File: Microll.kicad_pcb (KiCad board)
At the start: 2 copper layers, 41.1 x 57.9 mm, 35 parts, among them J1 Conn_02x08_Top_Bottom, J3 Conn_01x08, J4 USB_C_Receptacle, J5 Conn_01x08, SW1 SW_Push, SW2 SW_Push, SW3 SW_Push, U1 ESP32-C3-WROOM-02-N4, U2 TLV76733DRVx, U3 STM32G0B1CBU6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

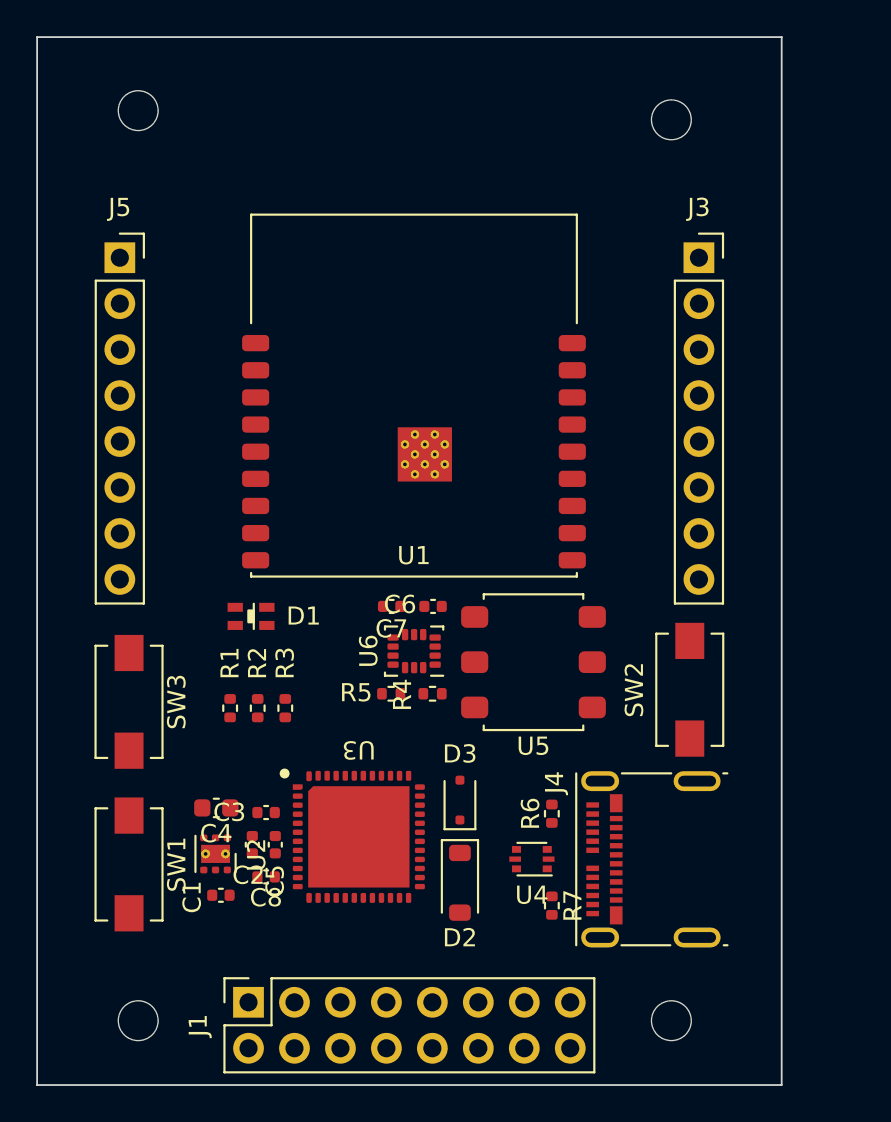
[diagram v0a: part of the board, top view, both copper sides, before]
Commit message: Changed the programming switches to a more compact dip format to save board space
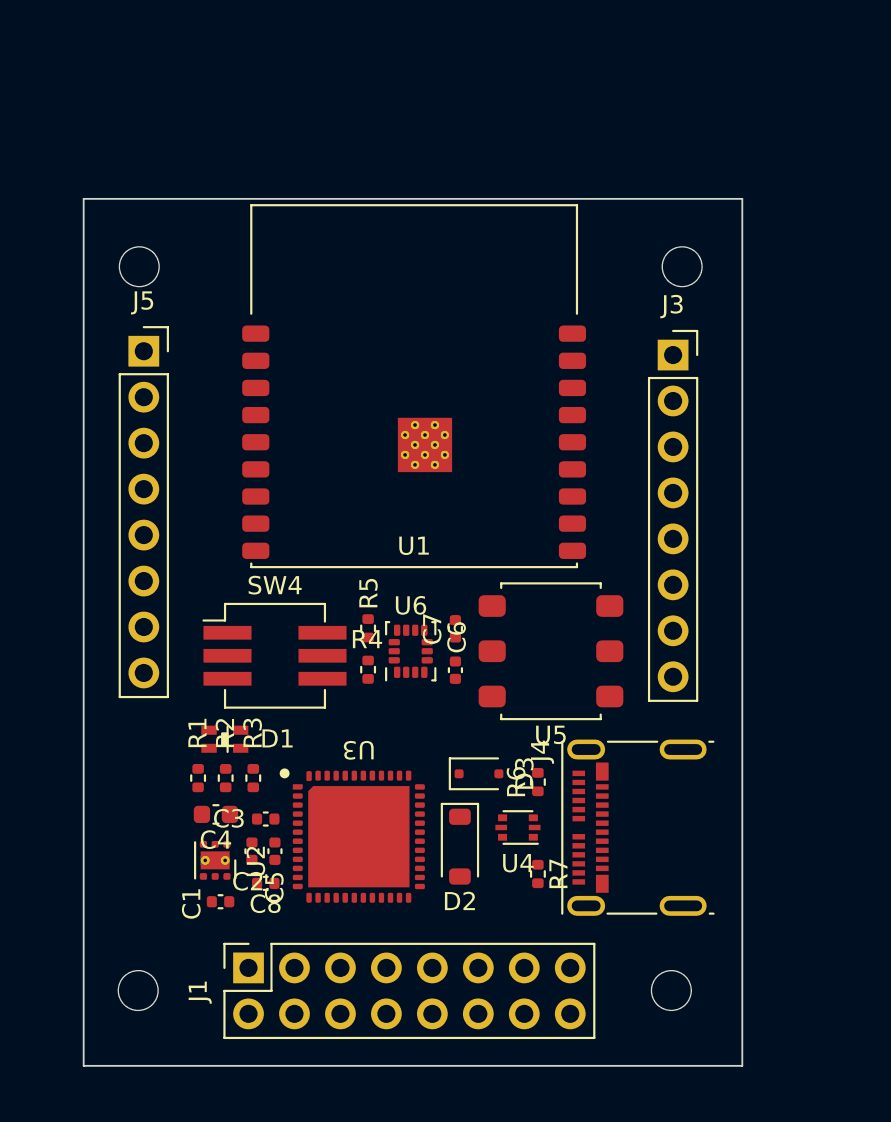
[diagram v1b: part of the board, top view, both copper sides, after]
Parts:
- removed SW1, SW2, SW3: SW_Push, Button_Switch_SMD:SW_SPST_EVQPE1
- added SW4: SW_DIP_x03, Button_Switch_SMD:SW_DIP_SPSTx03_Slide_KingTek_DSHP03TJ_W5.25mm_P1.27mm_JPin, F.Cu at (99.0, 69.8)
- moved H1 8.63 mm to (91.5, 48.2)
- moved H3 8.14 mm to (121.5, 48.2)
- moved D1 6.94 mm to (96.2, 74.4)
- moved J3 5.56 mm to (121.0, 53.1)
- moved J5 5.34 mm to (91.8, 52.9)
- moved R1 4.25 mm to (94.8, 76.5)
- moved R2 4.25 mm to (96.3, 76.5)
- moved R3 4.25 mm to (97.8, 76.5)
- moved R5 3.84 mm to (104.1, 68.2), turned to -90 degrees
- moved R4 3.80 mm to (104.1, 70.5), turned to 90 degrees
- moved C6 3.73 mm to (109.0, 70.5), turned to 90 degrees
- moved C7 3.73 mm to (109.0, 68.3), turned to -90 degrees
- moved D2 2.00 mm to (109.2, 80.3)
- moved J4 1.91 mm to (119.0, 79.2)
- moved R7 1.91 mm to (113.5, 81.8)
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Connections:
- U1 pad 2: +3.3V -> /EN
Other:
- board size 41.1 x 57.9 mm -> 36.4 x 47.9 mm

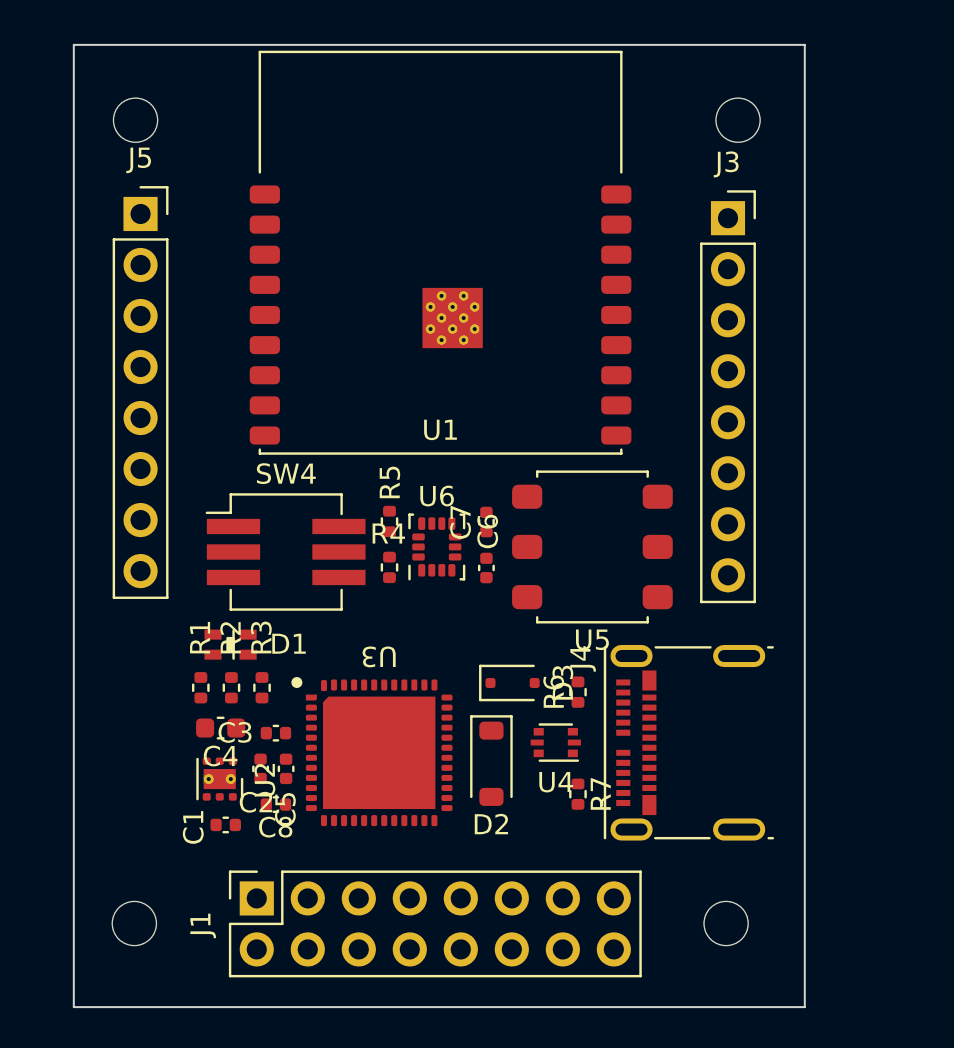
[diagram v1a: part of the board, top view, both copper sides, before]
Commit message: Board outline defined. Initial routing comenced
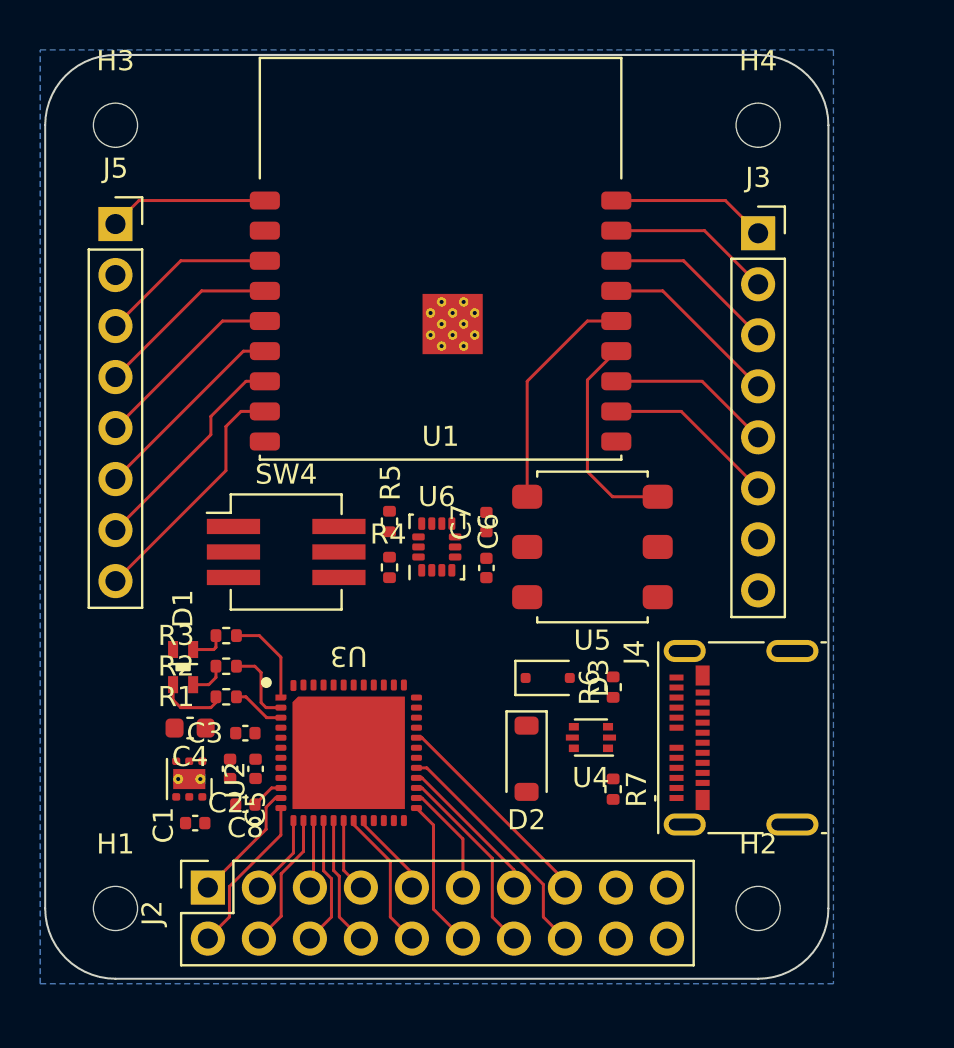
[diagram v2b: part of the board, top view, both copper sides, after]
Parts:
- removed J1: Conn_02x08_Top_Bottom, Connector_PinSocket_2.54mm:PinSocket_2x08_P2.54mm_Vertical
- added J2: Conn_02x10_Top_Bottom, Connector_PinSocket_2.54mm:PinSocket_2x10_P2.54mm_Vertical, F.Cu at (95.1, 86.5)
- moved H4 50.4 mm to (122.5, 48.5)
- moved H1 39.3 mm to (90.5, 87.5)
- moved H3 31.0 mm to (90.5, 48.5)
- moved R3 3.15 mm to (96.0, 73.9), turned to 0 degrees
- moved J4 2.66 mm to (121.7, 79.0)
- moved D1 2.61 mm to (93.9, 75.5), turned to 90 degrees
- moved D2 1.77 mm to (111.0, 80.0)
- moved D3 1.77 mm to (112.0, 76.0)
- moved R6 1.77 mm to (115.3, 76.5)
- moved R7 1.77 mm to (115.3, 81.6)
- moved U4 1.77 mm to (114.2, 79.0)
- moved H2 1.76 mm to (122.5, 87.5)
- moved J3 1.68 mm to (122.5, 53.9)
- moved C1 1.52 mm to (94.5, 83.2)
- moved C2 1.52 mm to (96.2, 80.5)
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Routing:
- net /GPIO9: track 0.00 -> 12.2 mm
- net USART_TX: track 0.00 -> 11.9 mm
- net ESP32_USB+: track 0.00 -> 11.4 mm
- net /GPIO8: track 0.00 -> 11.0 mm
- net USART_RX: track 0.00 -> 10.7 mm
- net ESP32_USB-: track 0.00 -> 10.6 mm
- net /GPIO7: track 0.00 -> 10.1 mm
- net /PB15: track 0.00 -> 9.67 mm
- net /GPIO6: track 0.00 -> 9.65 mm
- net SCL: track 0.00 -> 9.21 mm
- net /GPIO3: track 0.00 -> 9.03 mm
- net SDA: track 0.00 -> 8.78 mm
- net /Rx: track 0.00 -> 8.65 mm
- net /GPIO2: track 0.00 -> 8.60 mm
- net /Tx: track 0.00 -> 8.22 mm
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- added copper zone on B.Cu, net GND
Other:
- board size 36.4 x 47.9 mm -> 39 x 46 mm

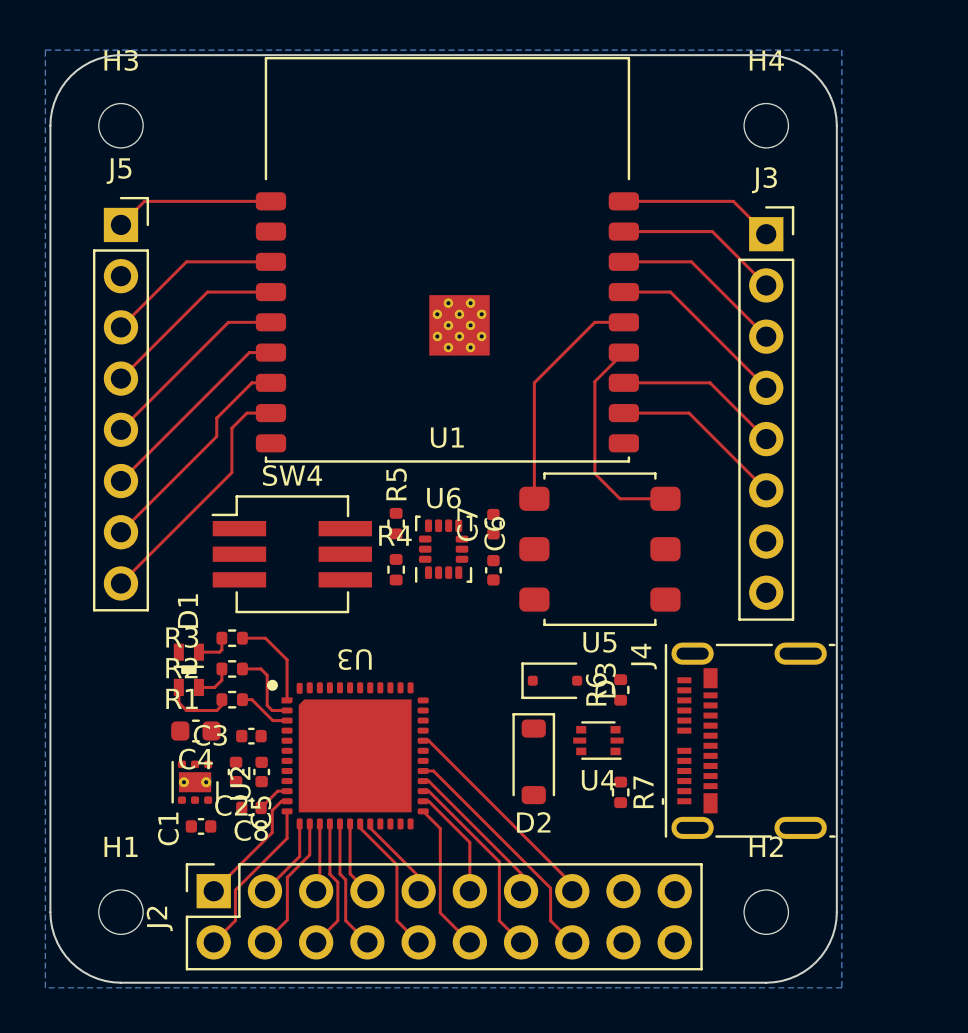
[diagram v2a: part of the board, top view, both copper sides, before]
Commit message: Additional routing. Need to update power symbols due tto kicad 8. Need to add 4 pins from STM32
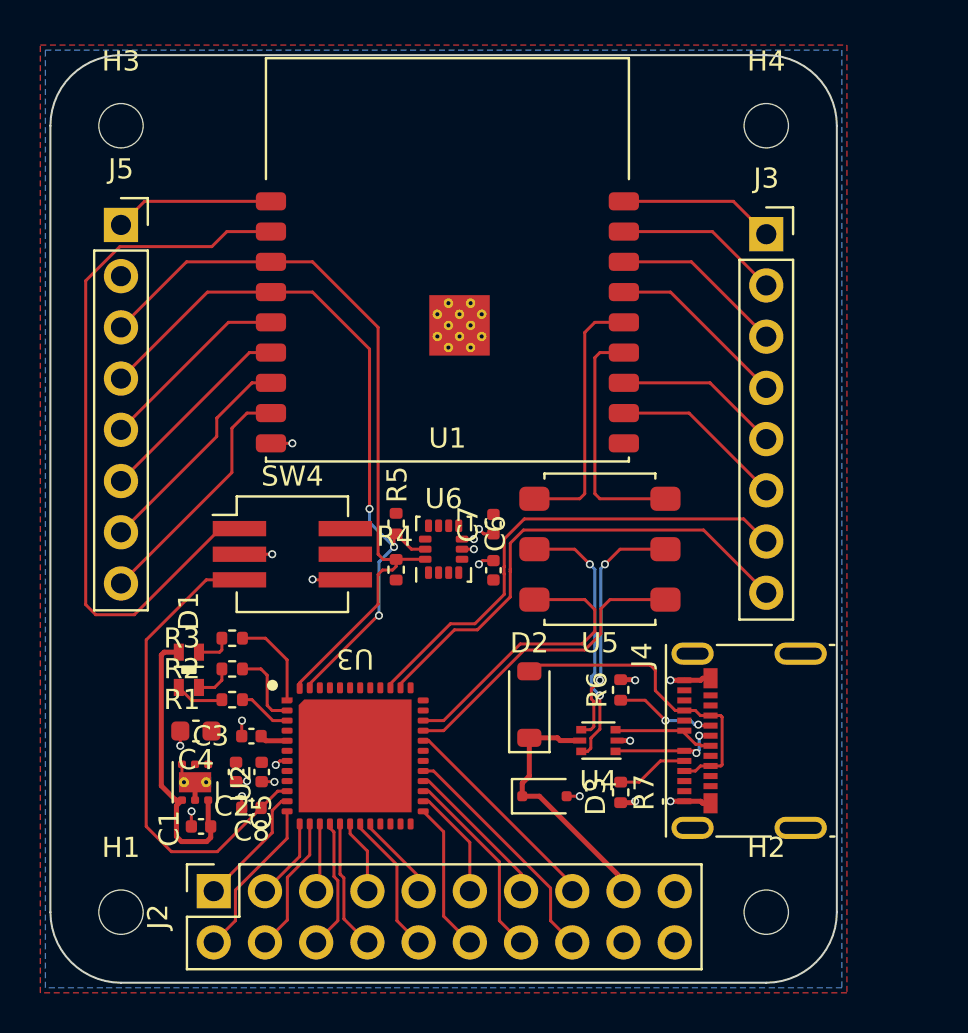
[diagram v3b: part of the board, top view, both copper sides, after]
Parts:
- moved D3 5.75 mm to (111.5, 81.8)
- moved D2 2.85 mm to (110.8, 77.2), turned to 90 degrees
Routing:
- net /EN: track 0.00 -> 35.9 mm
- net SDA: track 8.78 -> 37.8 mm
- net SCL: track 9.21 -> 36.8 mm, vias 0 -> 3
- net +5V: track 0.00 -> 27.3 mm
- net CAN_RX: track 0.00 -> 24.4 mm
- net CAN_TX: track 0.00 -> 24.3 mm
- net /RESET: track 1.63 -> 23.9 mm
- net GND: track 0.00 -> 20.5 mm, vias 0 -> 20
- net /5V_bus: track 0.00 -> 15.7 mm
- net STM32_USB-: track 0.00 -> 15.4 mm
- net STM32_USB+: track 0.00 -> 14.6 mm
- net /USB+: track 0.00 -> 13.3 mm, vias 0 -> 2
- net /USB-: track 0.00 -> 12.4 mm, vias 0 -> 2
- net /D+: track 0.00 -> 5.55 mm, vias 0 -> 2
- net /D-: track 0.00 -> 5.11 mm
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- added copper zone on F.Cu, net +3.3V
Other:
- board text added: "Remember to break out these 4 pins"

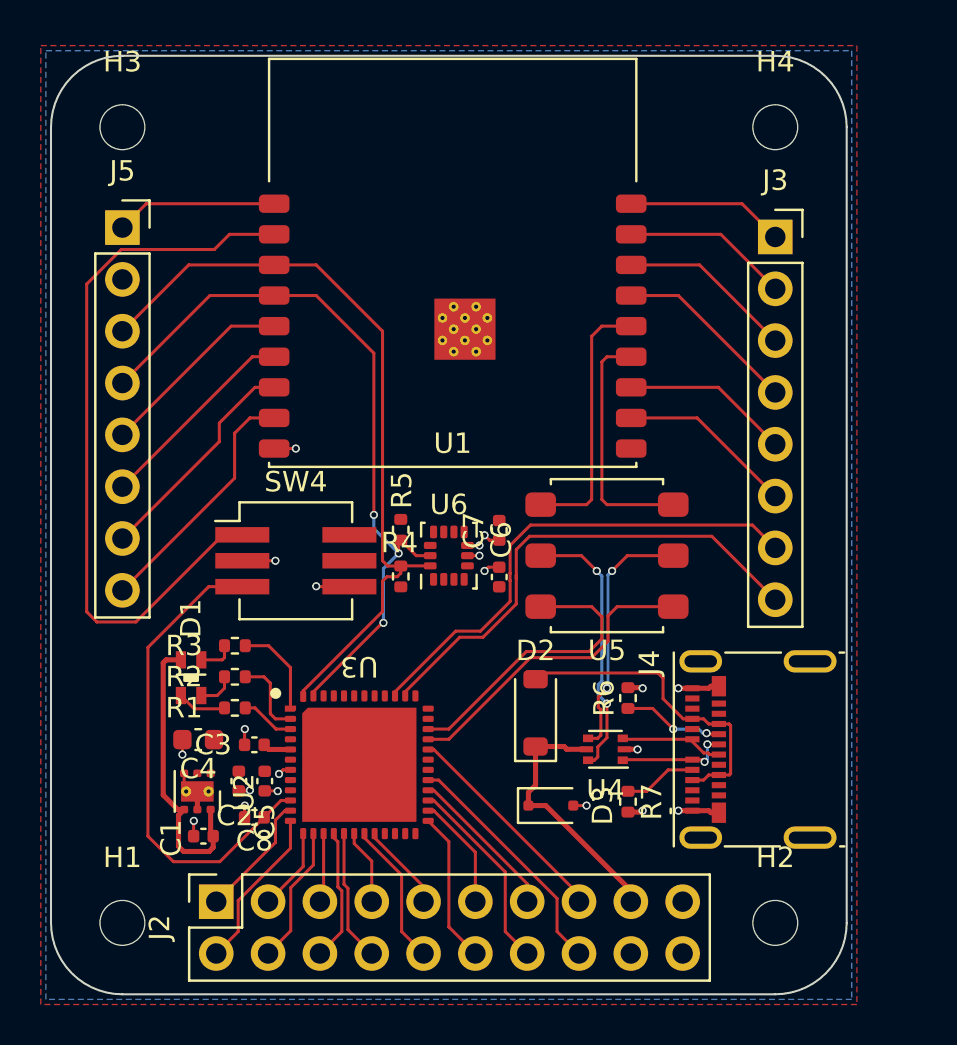
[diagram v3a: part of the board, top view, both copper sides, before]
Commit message: Largely finishhed routing. Need to sort out 3D model for USBC and add silk skreen pin labels to underside of board
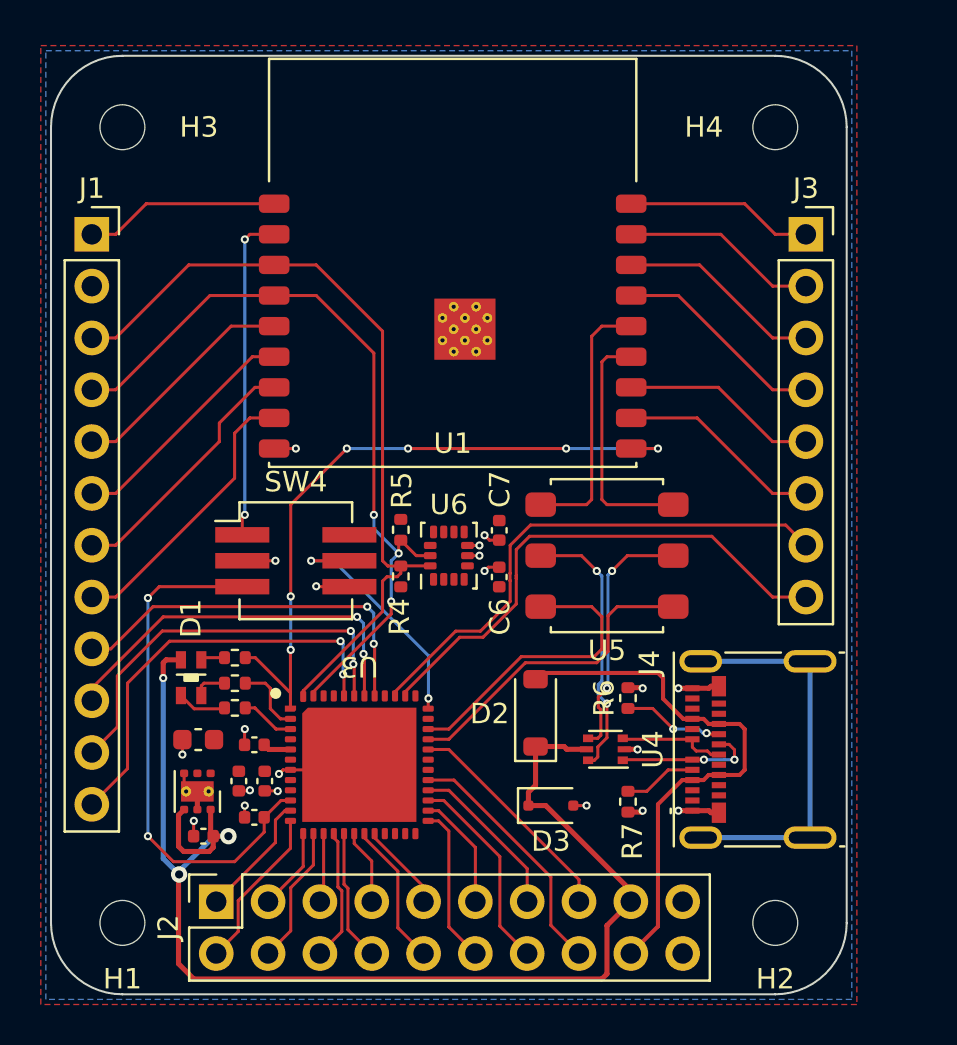
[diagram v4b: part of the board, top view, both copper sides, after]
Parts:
- removed J5: Conn_01x08, Connector_PinSocket_2.54mm:PinSocket_1x08_P2.54mm_Vertical
- added J1: Conn_01x12, Connector_PinSocket_2.54mm:PinSocket_1x12_P2.54mm_Vertical, F.Cu at (89.0, 53.8)
- moved J3 1.51 mm to (124.0, 53.8)
- moved R3 0.59 mm to (96.0, 74.5)
- moved R2 0.31 mm to (96.0, 75.8)
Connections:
- D2 pad 2: /5V_bus -> V_IN
- J4 pad A4: /5V_bus -> V_IN
- J4 pad A9: /5V_bus -> V_IN
- J4 pad B4: /5V_bus -> V_IN
- J4 pad B9: /5V_bus -> V_IN
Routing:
- net +5V: track 27.3 -> 64.1 mm, vias 0 -> 3
- net /Blue: track 4.67 -> 33.4 mm, vias 0 -> 6
- net V_IN: track 0.00 -> 26.9 mm
- net /PB5: track 0.00 -> 20.7 mm, vias 0 -> 2
- net /PB4: track 0.00 -> 19.9 mm, vias 0 -> 2
- net /EN: track 35.9 -> 16.1 mm, vias 0 -> 2
- net unconnected-(J4-SHIELD-PadS1)_2: track 0.00 -> 19.4 mm
- net /PB3: track 0.00 -> 19.1 mm, vias 0 -> 2
- net /PD3: track 0.00 -> 18.9 mm, vias 0 -> 2
- net /5V_bus: track 15.7 -> 0.00 mm
- net /BOOT: track 0.00 -> 12.2 mm, vias 0 -> 2
- net GND: track 20.5 -> 23.9 mm
- net /RESET: track 23.9 -> 25.7 mm, vias 0 -> 2
- net SDA: track 37.8 -> 39.4 mm
- net /GPIO9: track 12.2 -> 13.9 mm
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
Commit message: Updated USBC. Just need to add silkscreen to te bottom 12 pin connector and it's done
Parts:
- removed J4: USB_C_Receptacle, Connector_USB:USB_C_Receptacle_Molex_105450-0101
- added J6: USB_C_Receptacle_USB2.0_16P, Connector_USB:USB_C_Receptacle_GCT_USB4105-xx-A_16P_TopMnt_Horizontal, F.Cu at (122.2, 79.0)
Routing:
- net unconnected-(J4-SHIELD-PadS1)_2: track 19.4 -> 0.00 mm
- net GND: track 23.9 -> 22.0 mm
- net Net-(J6-CC2): track 4.98 -> 3.36 mm, vias 2 -> 0
- net V_IN: track 26.9 -> 25.6 mm
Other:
- board text added: "3.3V"
- board text added: "CAN_RX"
- board text added: "CAN_TX"
- board text added: "GND"
- board text added: "GPIO0"
- board text added: "GPIO1"
- board text added: "GPIO2"
- board text added: "GPIO3"
- board text added: "GPIO6"
- board text added: "GPIO7"
- board text added: "GPIO8"
- board text added: "GPIO9"
- board text added: "PB3"
- board text added: "PB4"
- board text added: "PB5"
- board text added: "PD3"
- board text added: "Rx"
- board text added: "SCL"
- board text added: "SDA"
- board text added: "Tx"
